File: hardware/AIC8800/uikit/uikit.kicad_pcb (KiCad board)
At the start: 2 copper layers, 50.8 x 69.2 mm, 40 parts, among them J1 Conn_01x20, J2 Conn_01x20, J3 Conn_01x10, J4 Conn_01x06, J5 USB_C_Receptacle_USB2.0, J6 Micro_SD_Card_Det, J7 PJ-393-USA, U1 AIC1000A, U2 CH340N

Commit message: [hardware/aic8800/uikit] update
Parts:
- moved R6 13.4 mm to (249.6, 131.4)
- moved C10 5.00 mm to (233.7, 126.4), turned to 0 degrees
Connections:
- C10 pad 1: /V33 -> /USB_3V
- R1 pad 2: /V33 -> /USB_3V
- R13 pad 1: Net-(R13-Pad1) -> Net-(U2-Pad2)
- U2 pad 1: Net-(R13-Pad1) -> Net-(R14-Pad1)
- U2 pad 2: Net-(R14-Pad1) -> Net-(U2-Pad2)
- U2 pad 5: /V33 -> /USB_5V
- U2 pad 8: /V33 -> /USB_3V
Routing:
- net /V33: track 54.1 -> 0.00 mm, vias 3 -> 0
- net /USB_5V: track 59.4 -> 71.1 mm
- net /USB_3V: track 0.00 -> 9.12 mm, vias 0 -> 2
- net Net-(U2-Pad2): track 0.00 -> 5.01 mm
- net Net-(R13-Pad1): track 4.49 -> 0.00 mm
- net Net-(J5-PadS1): track 3.74 -> 2.41 mm
- net Net-(R14-Pad1): track 4.49 -> 5.22 mm, vias 0 -> 2

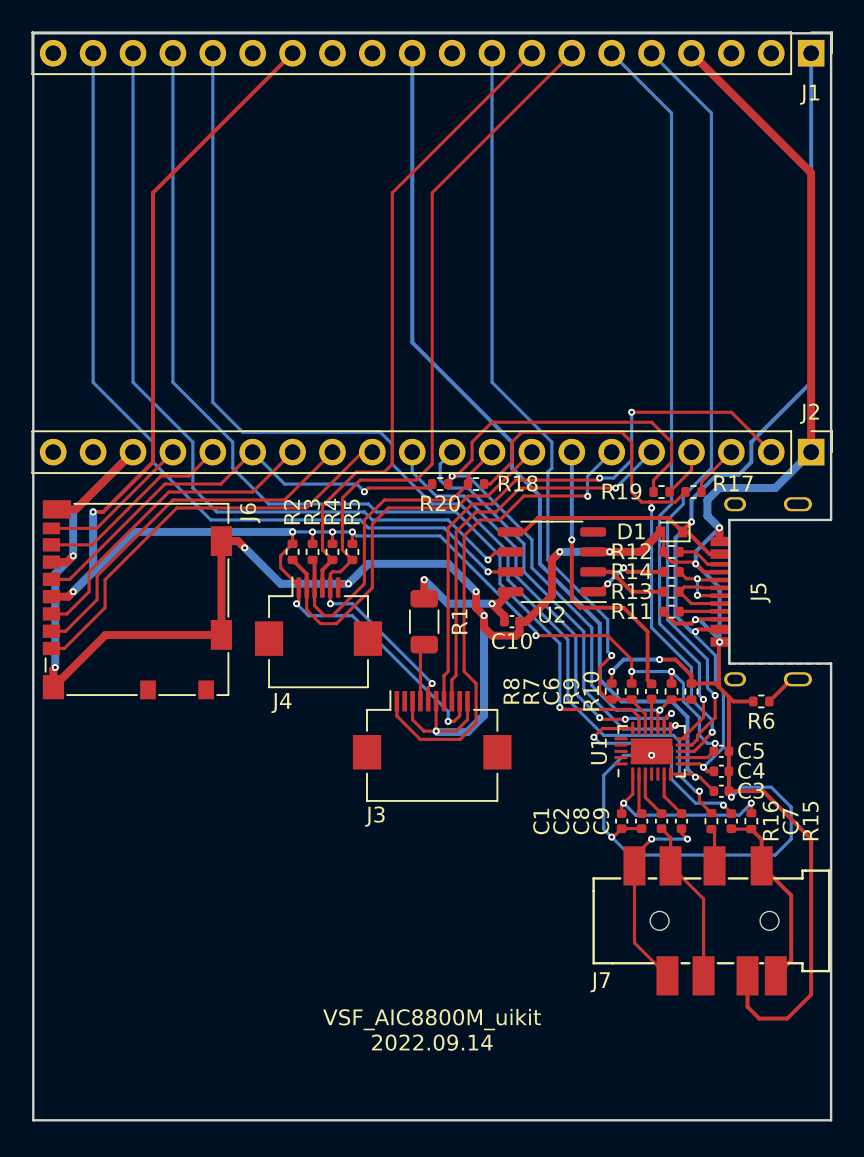
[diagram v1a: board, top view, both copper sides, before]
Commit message: [hardware/aic8800/uikit] PB6/PB7 can not be used as uart
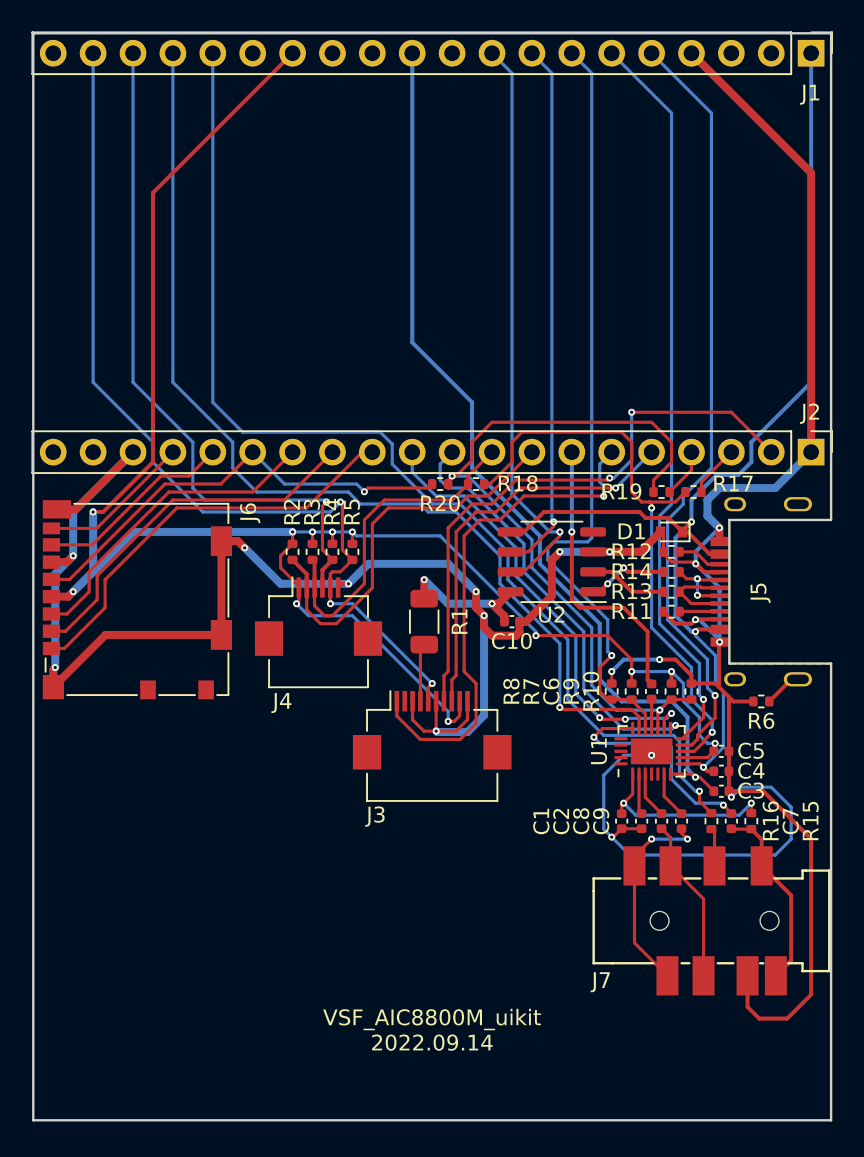
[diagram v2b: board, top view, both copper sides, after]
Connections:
- J1 pad 7: /B1 -> /AU_SLEEP
- J1 pad 9: /AU_SLEEP -> /B3
- J3 pad 6: /B1 -> /B7
- J4 pad 2: /B1 -> /B7
- J4 pad 3: /B2 -> /B6
- R4 pad 2: /B2 -> /B6
- R5 pad 2: /B1 -> /B7
- U2 pad 6: /B6 -> /B2
- U2 pad 7: /B7 -> /B3
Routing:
- net /B1: track 54.1 -> 0.00 mm, vias 2 -> 0
- net /B3: track 0.00 -> 37.0 mm, vias 0 -> 1
- net /B6: track 51.6 -> 44.2 mm
- net /B2: track 41.1 -> 34.3 mm, vias 0 -> 1
- net /B7: track 53.3 -> 58.6 mm, vias 1 -> 3
- net /AU_SLEEP: track 48.8 -> 50.0 mm
- net /A4: track 31.7 -> 32.5 mm

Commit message: [hardware/aic8800/uikit] add speaker
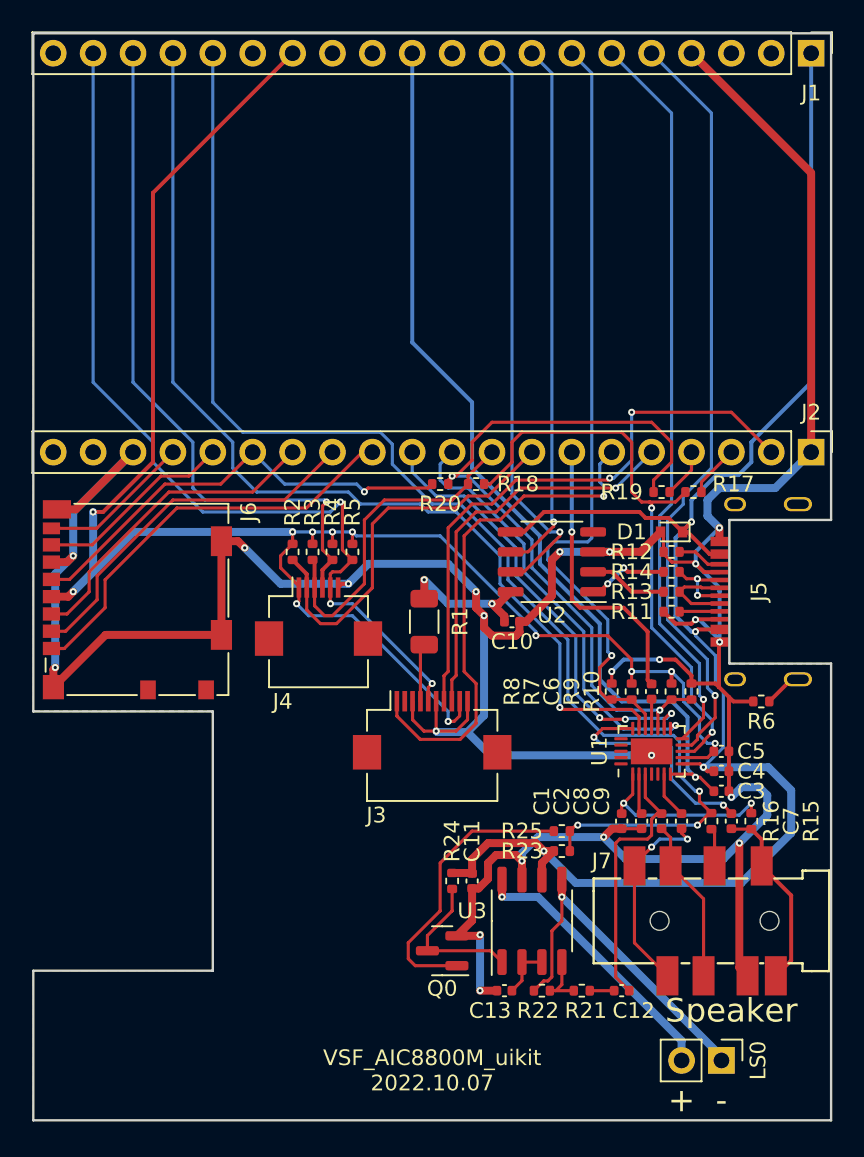
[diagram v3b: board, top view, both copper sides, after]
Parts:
- added C11: 0.1uF, Capacitor_SMD:C_0402_1005Metric, F.Cu at (231.1, 142.9)
- added C12: 0.39uF, Capacitor_SMD:C_0402_1005Metric, F.Cu at (240.7, 149.9)
- added C13: 0.1uF, Capacitor_SMD:C_0402_1005Metric, F.Cu at (233.2, 149.9)
- added LS0: Speaker, Connector_PinHeader_2.54mm:PinHeader_1x02_P2.54mm_Vertical, F.Cu at (247.0, 154.3)
- added Q0: S8050, Package_TO_SOT_SMD:SOT-23, F.Cu at (229.2, 147.3)
- added R21: 20K, Resistor_SMD:R_0402_1005Metric, F.Cu at (238.1, 149.9)
- added R22: 20K, Resistor_SMD:R_0402_1005Metric, F.Cu at (235.6, 149.9)
- added R23: 20K, Resistor_SMD:R_0402_1005Metric, F.Cu at (236.9, 141.0)
- added R24: 1K, Resistor_SMD:R_0402_1005Metric, F.Cu at (229.9, 142.9)
- added R25: 4.7K, Resistor_SMD:R_0402_1005Metric, F.Cu at (236.9, 139.7)
- added U3: NS8002, Package_SO:SOP-8_3.9x4.9mm_P1.27mm, F.Cu at (234.9, 145.4)
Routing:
- net /USB_5V: track 71.4 -> 108.4 mm, vias 3 -> 4
- net Net-(R22-Pad1): track 0.00 -> 22.6 mm, vias 0 -> 1
- net Net-(Q0-Pad1): track 0.00 -> 18.3 mm
- net Net-(LS0-Pad2): track 0.00 -> 17.6 mm, vias 0 -> 1
- net /HP_L+: track 2.94 -> 17.0 mm
- net /B4: track 70.5 -> 81.2 mm, vias 1 -> 3
- net Net-(Q0-Pad3): track 0.00 -> 9.63 mm
- net GND: track 232.9 -> 242.3 mm, vias 18 -> 22
- net Net-(R21-Pad1): track 0.00 -> 3.50 mm
- net Net-(U3-Pad2): track 0.00 -> 3.35 mm
- net Net-(C12-Pad2): track 0.00 -> 1.55 mm
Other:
- outline, holes or cut-outs redrawn
- board text added: "+"
- board text added: "-"
- board text added: "Speaker"
- board text added: "VSF_AIC8800M_uikit 2022.10.07"
- board text removed: "VSF_AIC8800M_uikit 2022.09.14"

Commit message: [hardware/aic8800/uikit] minor tweak
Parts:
- moved LS0 1.91 mm to (248.9, 154.3)
- moved C11 1.27 mm to (231.1, 144.1)
- moved Q0 1.27 mm to (229.2, 148.6)
- moved R23 1.27 mm to (236.9, 142.2)
- moved R24 1.27 mm to (229.9, 144.1)
- moved R25 1.27 mm to (236.9, 141.0)
- moved U3 1.27 mm to (234.9, 146.7)
- moved C12 1.27 mm to (240.7, 151.1)
- moved C13 1.27 mm to (233.2, 151.1)
- moved R21 1.27 mm to (238.1, 151.1)
- moved R22 1.27 mm to (235.6, 151.1)
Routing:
- net Net-(LS0-Pad2): track 17.6 -> 19.0 mm
- net /HP_L+: track 17.0 -> 18.3 mm
- net Net-(R22-Pad1): track 22.6 -> 23.8 mm
- net /USB_5V: track 108.4 -> 107.9 mm
- net /B4: track 81.2 -> 81.7 mm
- net GND: track 242.3 -> 242.8 mm

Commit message: [hardware/aic8800/uikit] fix i2s
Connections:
- R10 pad 2: /I2S_DIN -> /A9
- R9 pad 2: /I2S_DIN -> /A9
- U1 pad 14: /A9 -> /I2S_DIN
- U1 pad 15: /I2S_DIN -> /A9
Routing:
- net /I2S_DIN: track 47.0 -> 45.5 mm
- net /A9: track 28.9 -> 29.3 mm, vias 3 -> 2

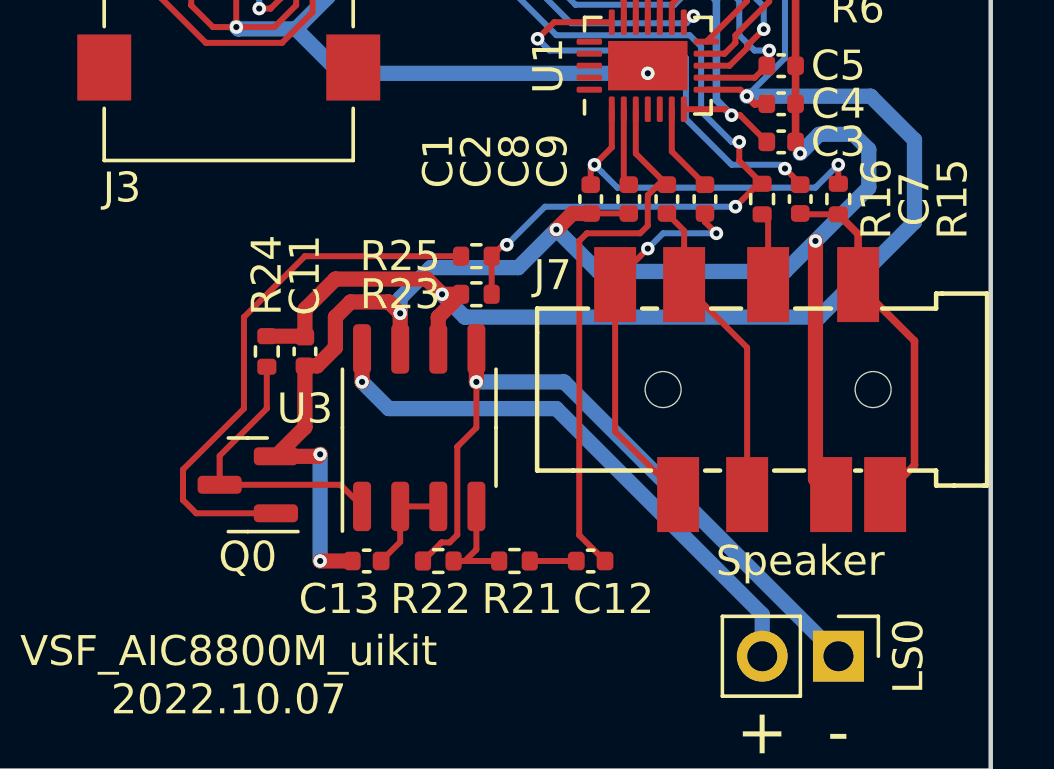
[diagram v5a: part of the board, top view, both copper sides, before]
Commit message: [hardware/aic8800/uikit] update JACK_DET
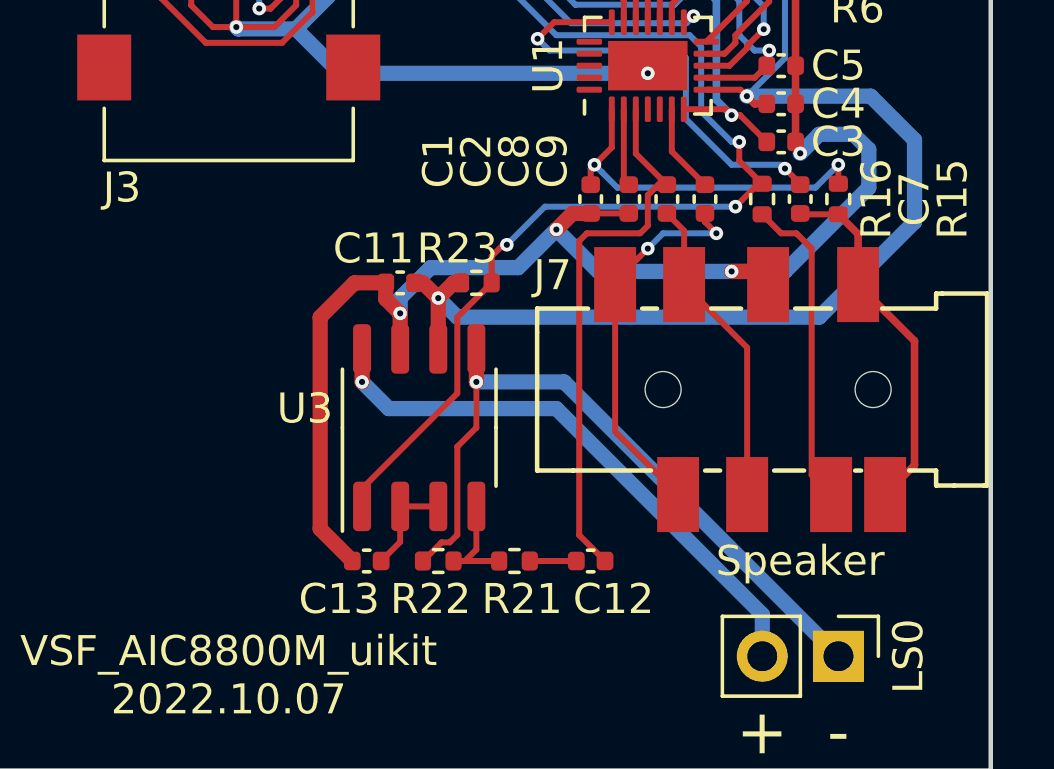
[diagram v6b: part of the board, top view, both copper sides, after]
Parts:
- removed Q0: S8050, Package_TO_SOT_SMD:SOT-23
- removed R24: 1K, Resistor_SMD:R_0402_1005Metric
- removed R25: 4.7K, Resistor_SMD:R_0402_1005Metric
- R23: value 20K -> 100K
- moved C11 3.91 mm to (234.3, 141.9), turned to 0 degrees
- moved R23 0.38 mm to (236.9, 141.9)
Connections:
- J7 pad 4: Net-(J7-Pad4) -> GND
- J7 pad 7: GND -> Net-(J7-Pad7)
- R16 pad 1: Net-(J7-Pad4) -> Net-(J7-Pad7)
- U3 pad 1: Net-(Q0-Pad3) -> /B4
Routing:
- net Net-(Q0-Pad1): track 18.3 -> 0.00 mm
- net Net-(J7-Pad7): track 0.00 -> 10.6 mm
- net Net-(Q0-Pad3): track 9.63 -> 0.00 mm
- net GND: track 242.8 -> 233.6 mm, vias 22 -> 20
- net /B4: track 81.7 -> 90.6 mm
- net /USB_5V: track 107.9 -> 101.5 mm
- net Net-(J7-Pad4): track 2.42 -> 0.00 mm

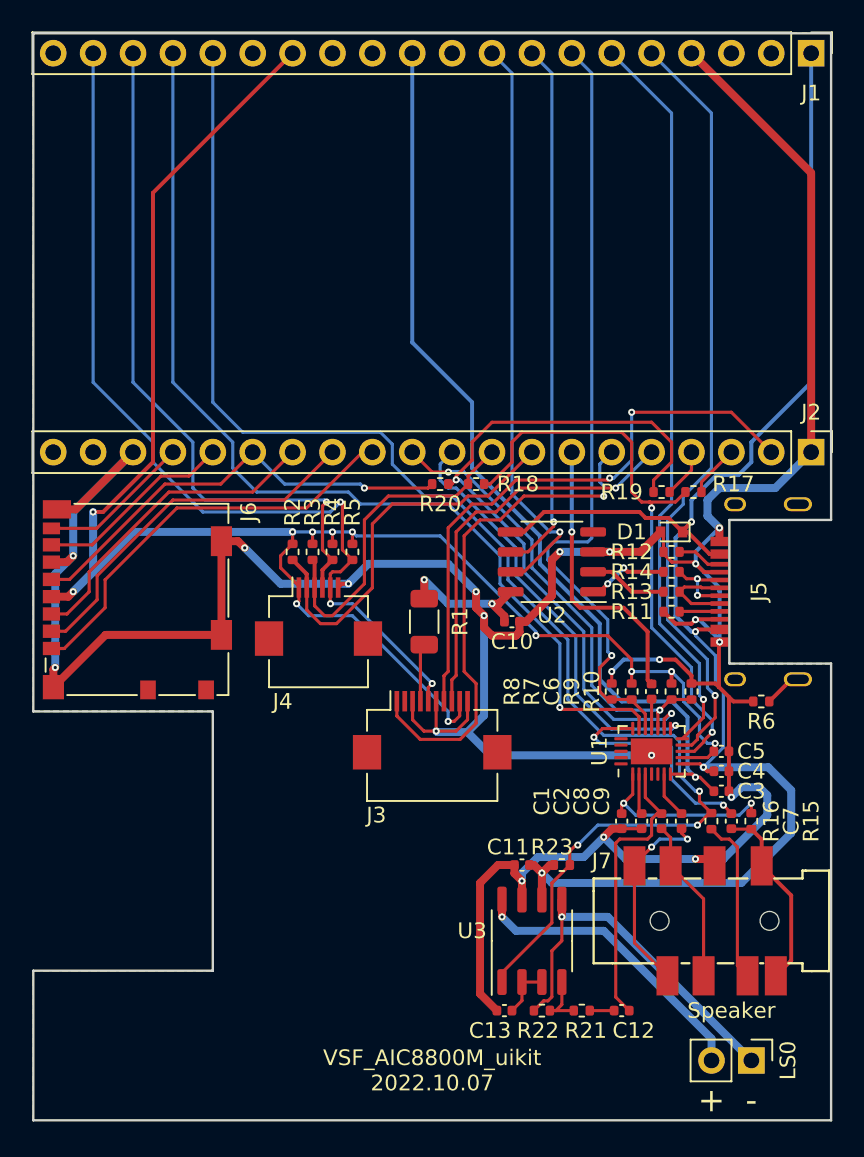
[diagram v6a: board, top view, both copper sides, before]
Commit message: [hardware/aic8800/uikit] PB0 can only be used as input
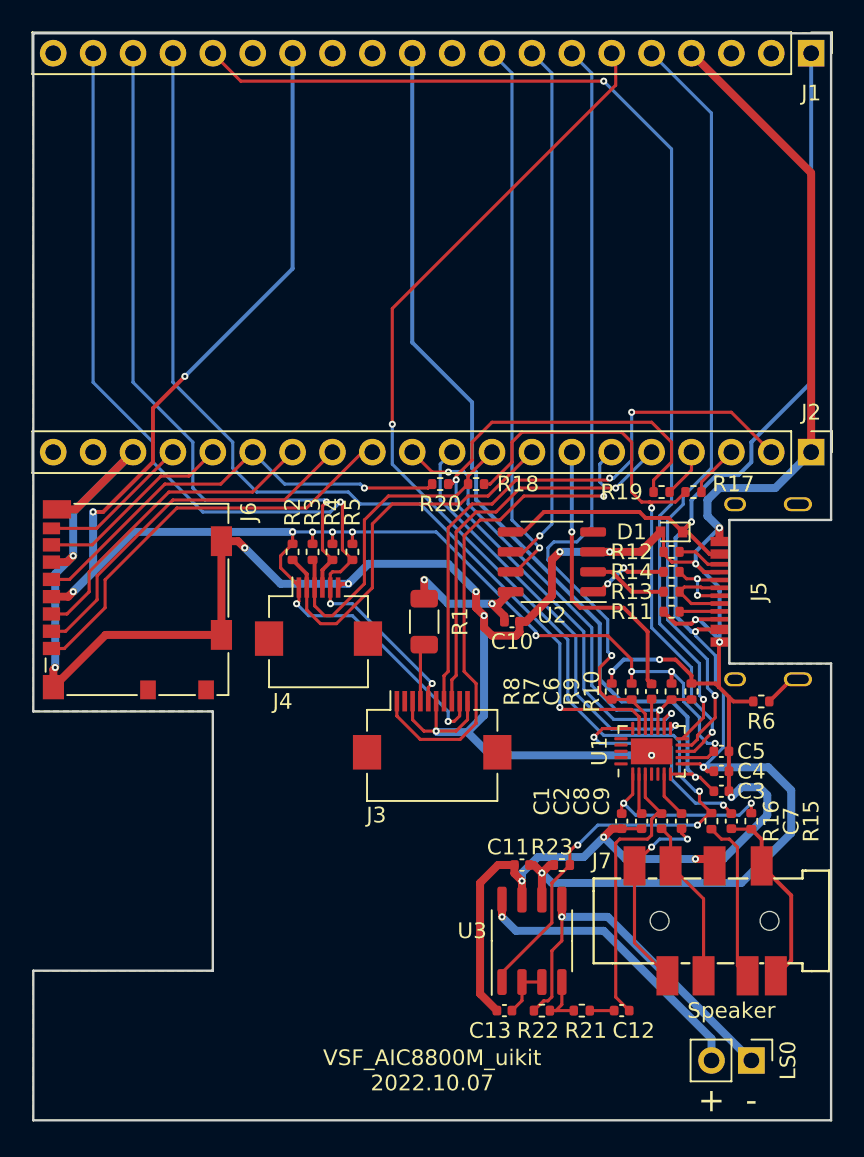
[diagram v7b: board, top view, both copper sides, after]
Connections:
- J1 pad 16: /B4 -> /AU_SCL
- J1 pad 6: /AU_SCL -> /B0
- R16 pad 2: /B4 -> /B0
- R23 pad 1: /B4 -> /B0
- U3 pad 1: /B4 -> /B0
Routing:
- net /B4: track 90.6 -> 0.00 mm, vias 3 -> 0
- net /B0: track 0.00 -> 85.7 mm, vias 0 -> 4
- net /AU_SCL: track 47.3 -> 71.3 mm, vias 1 -> 2
- net /B3: track 37.0 -> 35.3 mm
- net /AU_PWR: track 64.6 -> 63.6 mm
- net /VCC: vias 12 -> 13
